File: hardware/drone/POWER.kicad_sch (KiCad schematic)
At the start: 22 parts, among them IC101 TPS63000IDRCRQ1, J101 1769

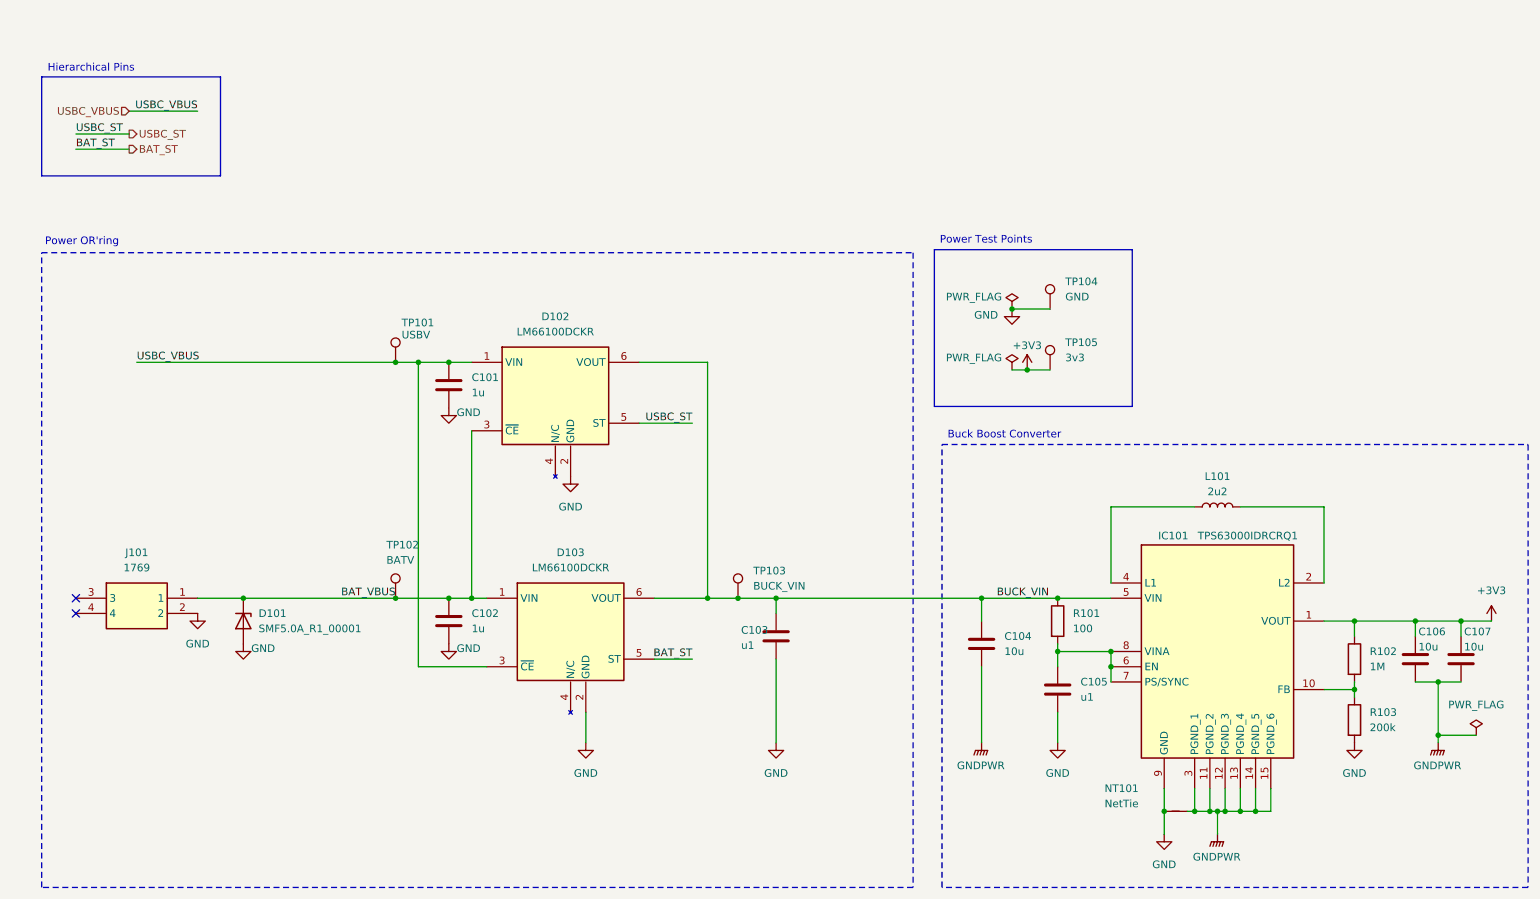
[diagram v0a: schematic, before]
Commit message: save before axing motor driver ic's
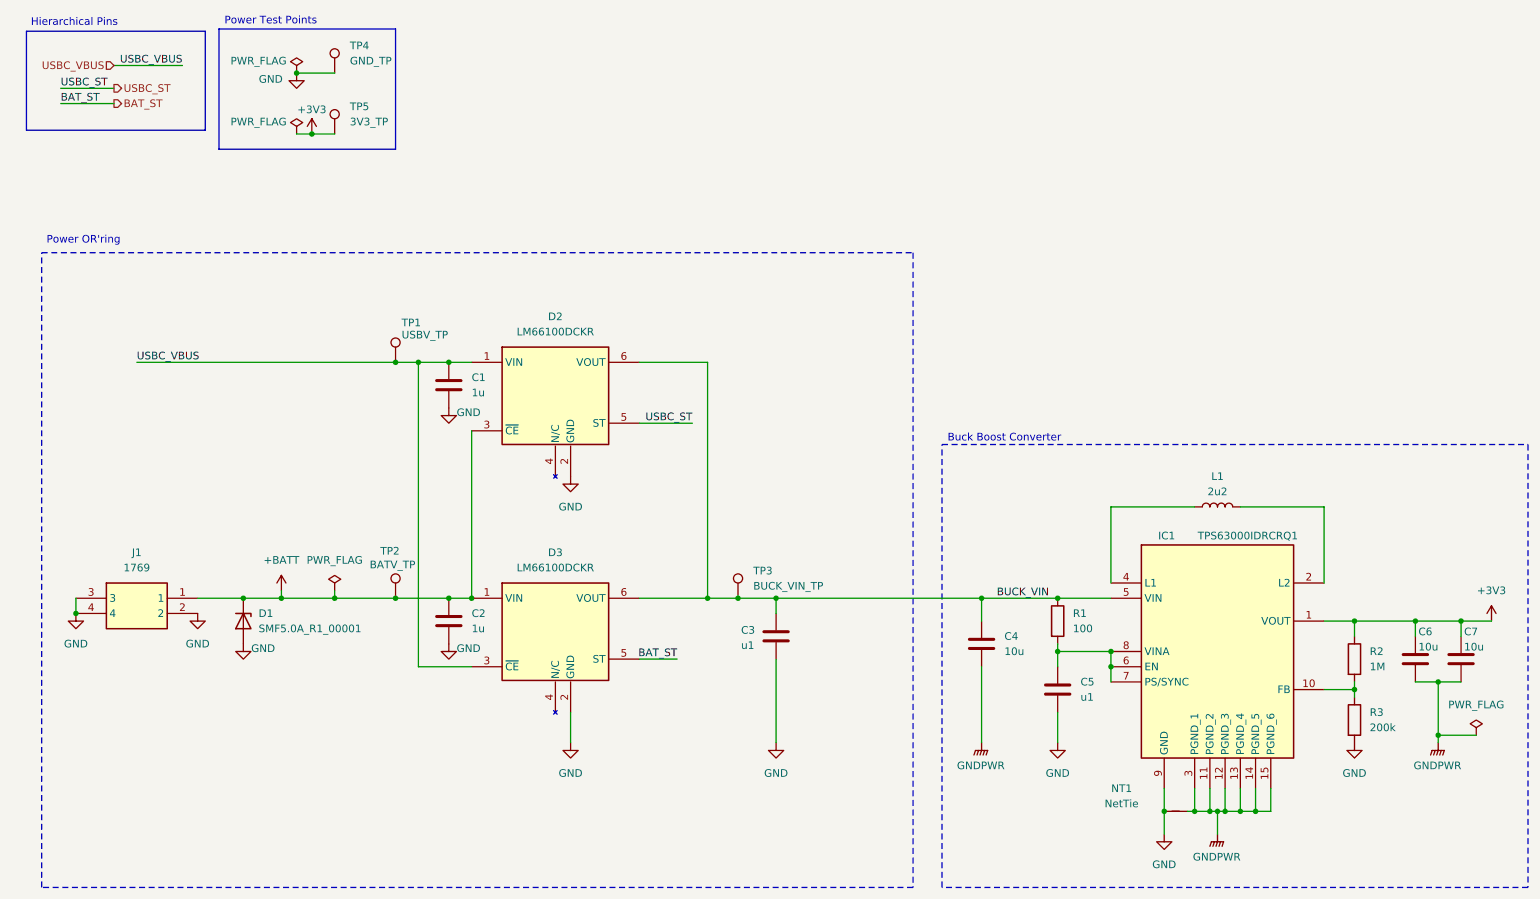
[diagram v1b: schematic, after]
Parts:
- NT1: renamed from NT101; footprint NetTie:NetTie-2_SMD_Pad0.5mm -> SamacSys_Parts:custom_net_tie
- R2: renamed from R102; Mouser Price/Stock https://www.mouser.com/ProductDetail/ROHM-Semiconductor/SFR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 -> https://www.mouser.co.uk/ProductDetail/ROHM-Semiconductor/S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
- TP1: renamed from TP101; value USBV -> USBV_TP; footprint TestPoint:TestPoint_Pad_1.0x1.0mm -> SamacSys_Parts:TestPoint_Pad_1.0x1.0mm
- TP2: renamed from TP102; value BATV -> BATV_TP; footprint TestPoint:TestPoint_Pad_1.0x1.0mm -> SamacSys_Parts:TestPoint_Pad_1.0x1.0mm
- TP3: renamed from TP103; value BUCK_VIN -> BUCK_VIN_TP; footprint TestPoint:TestPoint_Pad_1.0x1.0mm -> SamacSys_Parts:TestPoint_Pad_1.0x1.0mm
- TP4: renamed from TP104; value GND -> GND_TP; footprint TestPoint:TestPoint_Pad_1.0x1.0mm -> SamacSys_Parts:TestPoint_Pad_1.0x1.0mm
- TP5: renamed from TP105; value 3v3 -> 3V3_TP; footprint TestPoint:TestPoint_Pad_1.0x1.0mm -> SamacSys_Parts:TestPoint_Pad_1.0x1.0mm
- renumbered C101 to C1, C102 to C2, C103 to C3, C104 to C4, C105 to C5, C106 to C6, C107 to C7, D101 to D1, D102 to D2, D103 to D3, IC101 to IC1, J101 to J1, L101 to L1, R101 to R1, R103 to R3
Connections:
- net GND: now also J1.3, J1.4
- net BAT_VBUS renamed +BATT
- no-connect marks 2 -> 0
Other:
- moved on the sheet: D3, TP4, TP5

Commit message: axed motor drivers. finished layout for drone but need to review overall system design after reading some stuff
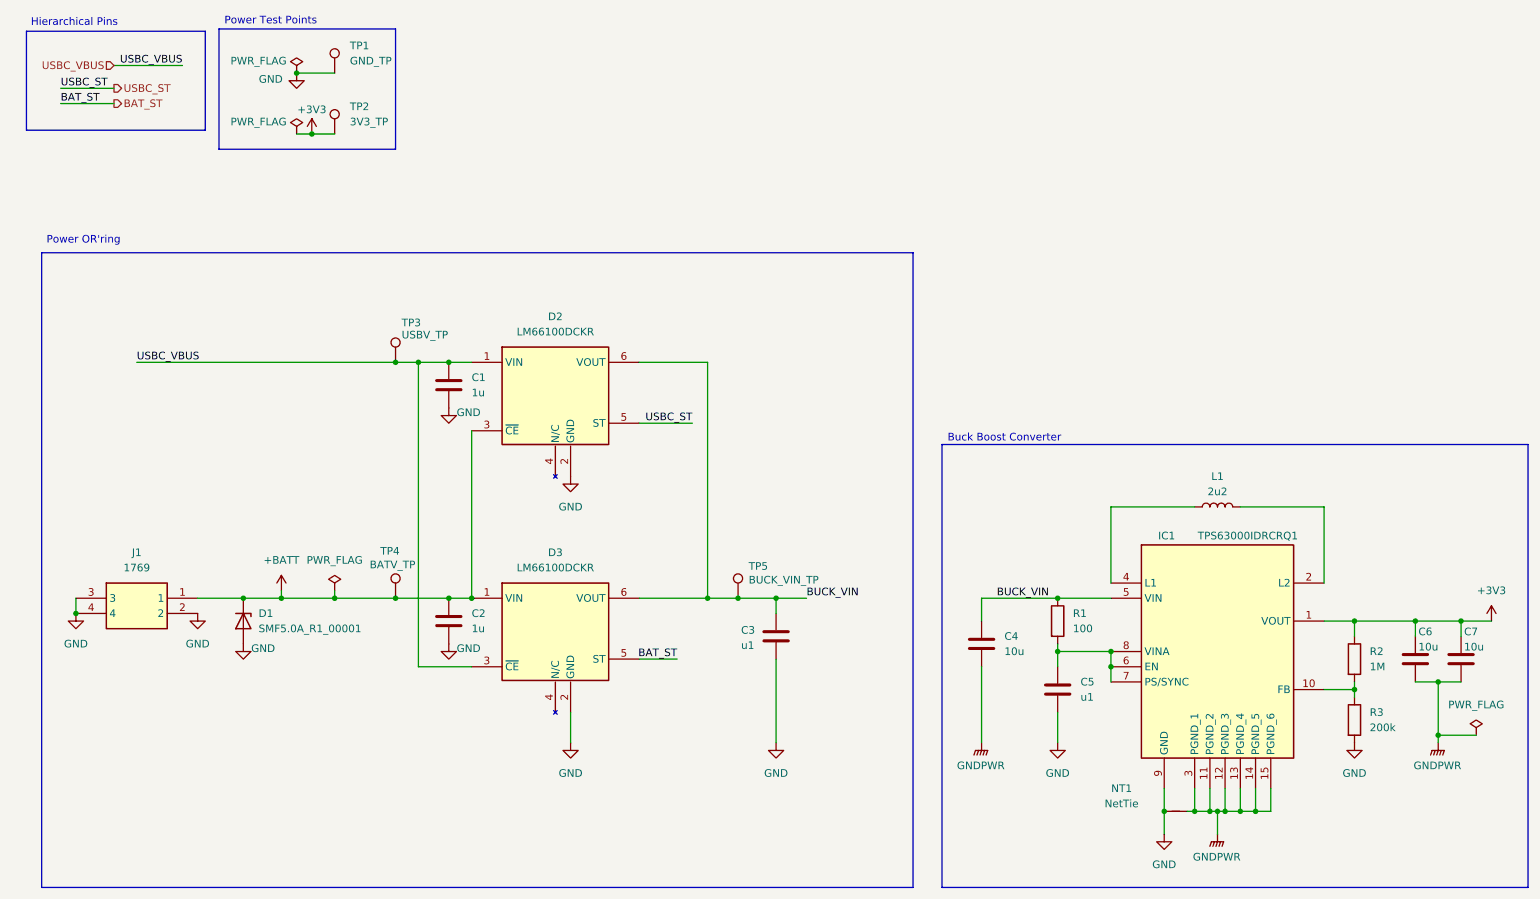
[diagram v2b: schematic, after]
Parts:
- R2: footprint Resistor_SMD:R_0603_1608Metric -> SamacSys_Parts:RESC1608X55N
- renumbered TP4 to TP1, TP5 to TP2, TP1 to TP3, TP2 to TP4, TP3 to TP5
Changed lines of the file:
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@@
 		(stroke
 			(width 0)
-			(type dash)
+			(type solid)
 		)
 		(fill
@@
 		(stroke
 			(width 0)
-			(type dash)
+			(type solid)
 		)
 		(fill
@@
 	)
 	(junction
-		(at 139.7 110.49)
-		(diameter 0)
-		(color 0 0 0 0)
-	)
-	(junction
 		(at 219.71 146.05)
 		(diameter 0)
@@
 	)
 	(junction
+		(at 139.7 110.49)
+		(diameter 0)
+		(color 0 0 0 0)
+	)
+	(junction
 		(at 246.38 114.3)
 		(diameter 0)
@@
 	)
 	(junction
-		(at 173.99 110.49)
-		(diameter 0)
-		(color 0 0 0 0)
-	)
-	(junction
 		(at 250.19 124.46)
 		(diameter 0)
@@
 	(wire
 		(pts
+			(xy 139.7 110.49) (xy 144.78 110.49)
+		)
+		(stroke
+			(width 0)
+			(type default)
+		)
+	)
+	(wire
+		(pts
 			(xy 20.32 27.94) (xy 29.21 27.94)
 		)
@@
 	(wire
 		(pts
-			(xy 139.7 110.49) (xy 173.99 110.49)
-		)
-		(stroke
-			(width 0)
-			(type default)
-		)
-	)
-	(wire
-		(pts
 			(xy 246.38 116.84) (xy 246.38 114.3)
 		)
@@
 		)
 	)
+	(label "BUCK_VIN"
+		(at 144.78 110.49 0)
+		(effects
+			(font
+				(size 1.27 1.27)
+			)
+			(justify left bottom)
+		)
+	)
 	(label "USBC_VBUS"
 		(at 40.64 21.59 180)
@@
 		(on_board yes)
 		(dnp no)
-		(property "Reference" "#PWR07"
+		(property "Reference" "#PWR011"
 			(at 85.09 85.09 0)
 			(effects
@@
 			(project "controller"
 				(path "/869bea87-c885-4ead-826b-3f34ceacafad/e70789ad-230b-4d46-b635-87f45083e468"
-					(reference "#PWR07")
+					(reference "#PWR011")
 					(unit 1)
 				)
@@
 		(dnp no)
 		(fields_autoplaced yes)
-		(property "Reference" "#PWR024"
+		(property "Reference" "#PWR08"
 			(at 57.15 113.03 0)
 			(effects
@@
 			(project "drone"
 				(path "/869bea87-c885-4ead-826b-3f34ceacafad/e70789ad-230b-4d46-b635-87f45083e468"
-					(reference "#PWR024")
+					(reference "#PWR08")
 					(unit 1)
 				)
@@
 		(on_board yes)
 		(dnp no)
-		(property "Reference" "#PWR06"
+		(property "Reference" "#PWR07"
 			(at 50.8 124.46 0)
 			(effects
@@
 			(project "controller"
 				(path "/869bea87-c885-4ead-826b-3f34ceacafad/e70789ad-230b-4d46-b635-87f45083e468"
-					(reference "#PWR06")
+					(reference "#PWR07")
 					(unit 1)
 				)
@@
 		(dnp no)
 		(fields_autoplaced yes)
-		(property "Reference" "TP4"
+		(property "Reference" "TP1"
 			(at 68.58 18.2879 0)
 			(effects
@@
 			(project ""
 				(path "/869bea87-c885-4ead-826b-3f34ceacafad/e70789ad-230b-4d46-b635-87f45083e468"
-					(reference "TP4")
+					(reference "TP1")
 					(unit 1)
 				)
@@
 			)
 		)
-		(property "Footprint" "Resistor_SMD:R_0603_1608Metric"
+		(property "Footprint" "SamacSys_Parts:RESC1608X55N"
 			(at 234.442 120.65 90)
 			(effects
@@
 		(on_board yes)
 		(dnp no)
-		(property "Reference" "#PWR08"
+		(property "Reference" "#PWR012"
 			(at 85.09 124.46 0)
 			(effects
@@
 			(project "controller"
 				(path "/869bea87-c885-4ead-826b-3f34ceacafad/e70789ad-230b-4d46-b635-87f45083e468"
-					(reference "#PWR08")
+					(reference "#PWR012")
 					(unit 1)
 				)
@@
 		(dnp no)
 		(fields_autoplaced yes)
-		(property "Reference" "#PWR09"
+		(property "Reference" "#PWR013"
 			(at 105.41 96.52 0)
 			(effects
@@
 			(project ""
 				(path "/869bea87-c885-4ead-826b-3f34ceacafad/e70789ad-230b-4d46-b635-87f45083e468"
-					(reference "#PWR09")
+					(reference "#PWR013")
 					(unit 1)
 				)
@@
 		(dnp no)
 		(fields_autoplaced yes)
-		(property "Reference" "#PWR05"
+		(property "Reference" "#PWR06"
 			(at 43.18 119.38 0)
 			(effects
@@
 			(project ""
 				(path "/869bea87-c885-4ead-826b-3f34ceacafad/e70789ad-230b-4d46-b635-87f45083e468"
-					(reference "#PWR05")
+					(reference "#PWR06")
 					(unit 1)
 				)
@@
 		(on_board yes)
 		(dnp no)
-		(property "Reference" "#PWR013"
+		(property "Reference" "#PWR09"
 			(at 59.69 29.21 0)
 			(effects
@@
 			(project "controller"
 				(path "/869bea87-c885-4ead-826b-3f34ceacafad/e70789ad-230b-4d46-b635-87f45083e468"
-					(reference "#PWR013")
+					(reference "#PWR09")
 					(unit 1)
 				)
@@
 		(dnp no)
 		(fields_autoplaced yes)
-		(property "Reference" "#PWR019"
+		(property "Reference" "#PWR021"
 			(at 250.19 139.7 0)
 			(effects
@@
 			(project "controller"
 				(path "/869bea87-c885-4ead-826b-3f34ceacafad/e70789ad-230b-4d46-b635-87f45083e468"
-					(reference "#PWR019")
+					(reference "#PWR021")
 					(unit 1)
 				)
@@
 		(on_board yes)
 		(dnp no)
-		(property "Reference" "TP2"
+		(property "Reference" "TP4"
 			(at 73.66 102.616 0)
 			(effects
@@
 			(project "controller"
 				(path "/869bea87-c885-4ead-826b-3f34ceacafad/e70789ad-230b-4d46-b635-87f45083e468"
-					(reference "TP2")
+					(reference "TP4")
 					(unit 1)
 				)
@@
 		(dnp no)
 		(fields_autoplaced yes)
-		(property "Reference" "#PWR010"
+		(property "Reference" "#PWR014"
 			(at 105.41 140.97 0)
 			(effects
@@
 			(project "controller"
 				(path "/869bea87-c885-4ead-826b-3f34ceacafad/e70789ad-230b-4d46-b635-87f45083e468"
-					(reference "#PWR010")
+					(reference "#PWR014")
 					(unit 1)
 				)
@@
 		(dnp no)
 		(fields_autoplaced yes)
-		(property "Reference" "#FLG03"
+		(property "Reference" "#FLG04"
 			(at 256.54 131.445 0)
 			(effects
@@
 			(project ""
 				(path "/869bea87-c885-4ead-826b-3f34ceacafad/e70789ad-230b-4d46-b635-87f45083e468"
-					(reference "#FLG03")
+					(reference "#FLG04")
 					(unit 1)
 				)
@@
 		(dnp no)
 		(fields_autoplaced yes)
-		(property "Reference" "#PWR018"
+		(property "Reference" "#PWR020"
 			(at 236.22 140.97 0)
 			(effects
@@
 			(project "controller"
 				(path "/869bea87-c885-4ead-826b-3f34ceacafad/e70789ad-230b-4d46-b635-87f45083e468"
-					(reference "#PWR018")
+					(reference "#PWR020")
 					(unit 1)
 				)
@@
 		(dnp no)
 		(fields_autoplaced yes)
-		(property "Reference" "#FLG06"
+		(property "Reference" "#FLG03"
 			(at 66.04 107.315 0)
 			(effects
@@
 			(project ""
 				(path "/869bea87-c885-4ead-826b-3f34ceacafad/e70789ad-230b-4d46-b635-87f45083e468"
-					(reference "#FLG06")
+					(reference "#FLG03")
 					(unit 1)
 				)
@@
 		(on_board yes)
 		(dnp no)
-		(property "Reference" "TP1"
+		(property "Reference" "TP3"
 			(at 77.216 64.516 0)
 			(effects
@@
 			(project "controller"
 				(path "/869bea87-c885-4ead-826b-3f34ceacafad/e70789ad-230b-4d46-b635-87f45083e468"
-					(reference "TP1")
+					(reference "TP3")
 					(unit 1)
 				)
@@
 		(dnp no)
 		(fields_autoplaced yes)
-		(property "Reference" "#PWR017"
+		(property "Reference" "#PWR019"
 			(at 213.36 154.94 0)
 			(effects
@@
 			(project ""
 				(path "/869bea87-c885-4ead-826b-3f34ceacafad/e70789ad-230b-4d46-b635-87f45083e468"
-					(reference "#PWR017")
+					(reference "#PWR019")
 					(unit 1)
 				)
@@
 		(dnp no)
 		(fields_autoplaced yes)
-		(property "Reference" "#PWR016"
+		(property "Reference" "#PWR018"
 			(at 204.47 156.21 0)
 			(effects
@@
 			(project ""
 				(path "/869bea87-c885-4ead-826b-3f34ceacafad/e70789ad-230b-4d46-b635-87f45083e468"
-					(reference "#PWR016")
+					(reference "#PWR018")
 					(unit 1)
 				)
@@
 		(dnp no)
 		(fields_autoplaced yes)
-		(property "Reference" "#PWR011"
+		(property "Reference" "#PWR015"
 			(at 139.7 140.97 0)
 			(effects
@@
 			(project "controller"
 				(path "/869bea87-c885-4ead-826b-3f34ceacafad/e70789ad-230b-4d46-b635-87f45083e468"
-					(reference "#PWR011")
+					(reference "#PWR015")
 					(unit 1)
 				)
@@
 		(dnp no)
 		(fields_autoplaced yes)
-		(property "Reference" "#PWR012"
+		(property "Reference" "#PWR016"
 			(at 173.99 139.7 0)
 			(effects
@@
 			(project "controller"
 				(path "/869bea87-c885-4ead-826b-3f34ceacafad/e70789ad-230b-4d46-b635-87f45083e468"
-					(reference "#PWR012")
+					(reference "#PWR016")
 					(unit 1)
 				)
@@
 		(dnp no)
 		(fields_autoplaced yes)
-		(property "Reference" "#PWR066"
+		(property "Reference" "#PWR05"
 			(at 22.86 119.38 0)
 			(effects
@@
 			(project "drone"
 				(path "/869bea87-c885-4ead-826b-3f34ceacafad/e70789ad-230b-4d46-b635-87f45083e468"
-					(reference "#PWR066")
+					(reference "#PWR05")
 					(unit 1)
 				)
@@
 		(on_board yes)
 		(dnp no)
-		(property "Reference" "#PWR014"
+		(property "Reference" "#PWR010"
 			(at 62.23 36.83 0)
 			(effects
@@
 			(project ""
 				(path "/869bea87-c885-4ead-826b-3f34ceacafad/e70789ad-230b-4d46-b635-87f45083e468"
-					(reference "#PWR014")
+					(reference "#PWR010")
 					(unit 1)
 				)
@@
 		(dnp no)
 		(fields_autoplaced yes)
-		(property "Reference" "#PWR020"
+		(property "Reference" "#PWR022"
 			(at 259.08 118.11 0)
 			(effects
@@
 			(project ""
 				(path "/869bea87-c885-4ead-826b-3f34ceacafad/e70789ad-230b-4d46-b635-87f45083e468"
-					(reference "#PWR020")
+					(reference "#PWR022")
 					(unit 1)
 				)
@@
 		(dnp no)
 		(fields_autoplaced yes)
-		(property "Reference" "#PWR015"
+		(property "Reference" "#PWR017"
 			(at 186.69 140.97 0)
 			(effects
@@
 			(project "controller"
 				(path "/869bea87-c885-4ead-826b-3f34ceacafad/e70789ad-230b-4d46-b635-87f45083e468"
-					(reference "#PWR015")
+					(reference "#PWR017")
 					(unit 1)
 				)
@@
 		(on_board yes)
 		(dnp no)
-		(fields_autoplaced yes)
-		(property "Reference" "TP3"
-			(at 135.89 105.9179 0)
+		(property "Reference" "TP5"
+			(at 135.128 105.156 0)
 			(effects
 				(font
@@
 		)
 		(property "Value" "BUCK_VIN_TP"
-			(at 135.89 108.4579 0)
+			(at 135.128 107.442 0)
 			(effects
 				(font
@@
 			(project "controller"
 				(path "/869bea87-c885-4ead-826b-3f34ceacafad/e70789ad-230b-4d46-b635-87f45083e468"
-					(reference "TP3")
+					(reference "TP5")
 					(unit 1)
 				)
@@
 		(dnp no)
 		(fields_autoplaced yes)
-		(property "Reference" "TP5"
+		(property "Reference" "TP2"
 			(at 68.58 28.4479 0)
 			(effects
@@
 			(project "controller"
 				(path "/869bea87-c885-4ead-826b-3f34ceacafad/e70789ad-230b-4d46-b635-87f45083e468"
-					(reference "TP5")
+					(reference "TP2")
 					(unit 1)
 				)
